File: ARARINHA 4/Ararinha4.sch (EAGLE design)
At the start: 105 parts, among them IC1 4053N, Q1 BC548, Q2 BC548, Q3 BC548, Q4 BC548, Q5 BC548, Q6 BC548, T1 TOROID-T37-4PIN, T2 TOROID-T37-4PIN, U1 LM386

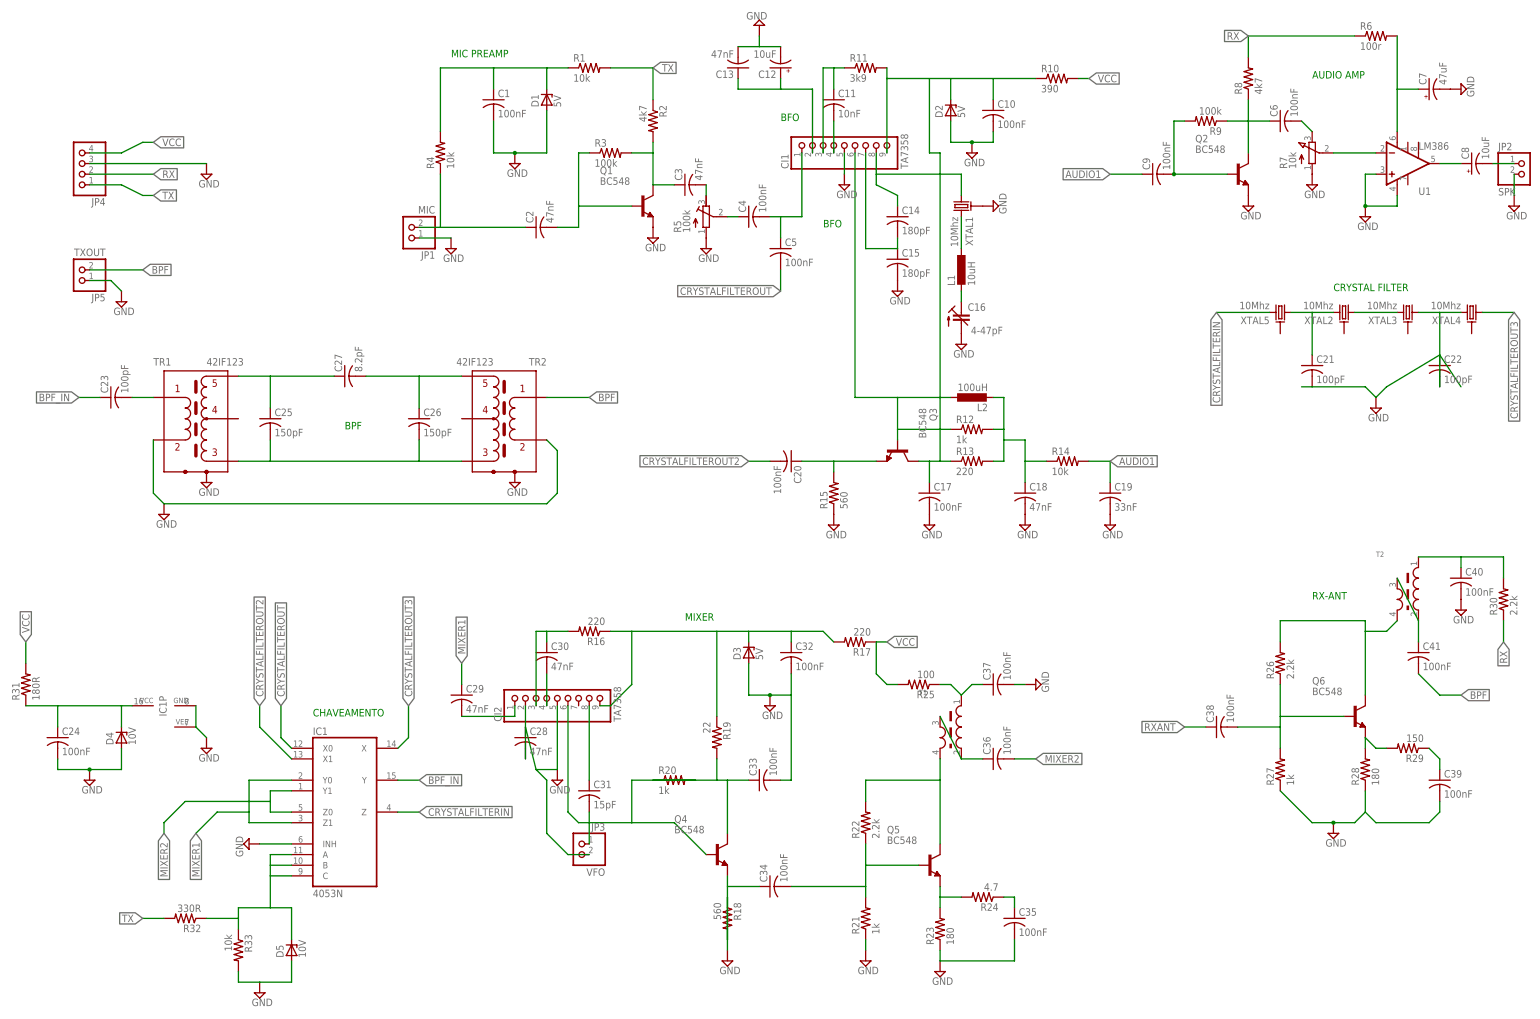
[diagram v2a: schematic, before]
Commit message: 
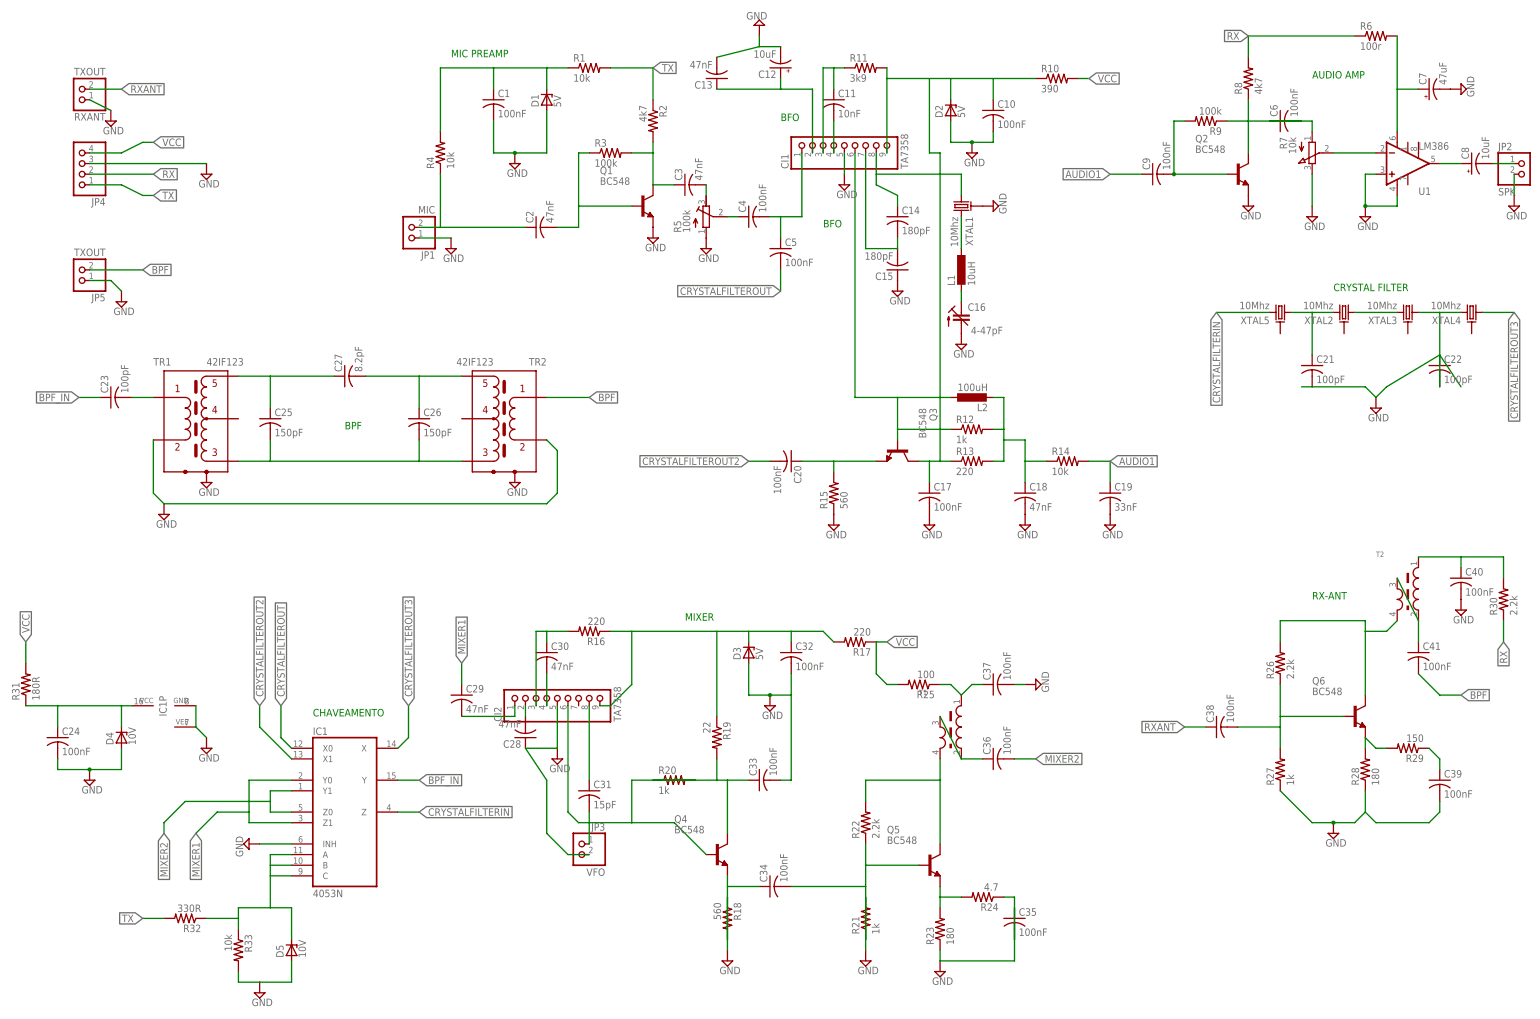
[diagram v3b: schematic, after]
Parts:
- added RXANT: TXOUT, pinhead:PINHD-1X2
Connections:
- removed net N$13 (its old number): C6.2, R7.E
- new net N$10: C6.1, R7.A
- net GND: now also C15.1, C35.1, R21.2, R7.E, RXANT.1; no longer C15.2, C35.2, R21.1, R7.A
- net N$14: now also C6.2; no longer C6.1
- net N$21: now also C15.2; no longer C15.1
- net N$43: now also C35.2; no longer C35.1
- net N$46: now also R21.1; no longer R21.2
- net RXANT: now also RXANT.2
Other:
- moved on the sheet: C13, C15, C28, R7
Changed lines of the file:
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@@
 <part name="SUPPLY36" library="supply2" deviceset="GND" device=""/>
 <part name="SUPPLY37" library="supply2" deviceset="GND" device=""/>
+<part name="RXANT" library="pinhead" deviceset="PINHD-1X2" device="" value="TXOUT"/>
+<part name="SUPPLY38" library="supply2" deviceset="GND" device=""/>
 </parts>
 <sheets>
@@
 <instance part="R6" gate="G$1" x="162.56" y="99.06"/>
 <instance part="C6" gate="G$1" x="139.7" y="78.74" rot="R90"/>
-<instance part="R7" gate="G$1" x="147.32" y="71.12"/>
+<instance part="R7" gate="G$1" x="147.32" y="71.12" rot="MR180"/>
 <instance part="C7" gate="G$1" x="175.26" y="86.36" rot="R90"/>
 <instance part="SUPPLY6" gate="GND" x="182.88" y="86.36" rot="R90"/>
@@
 <instance part="R9" gate="G$1" x="121.92" y="78.74" rot="R180"/>
 <instance part="SUPPLY8" gate="GND" x="132.08" y="58.42"/>
-<instance part="SUPPLY9" gate="GND" x="147.32" y="63.5"/>
+<instance part="SUPPLY9" gate="GND" x="147.32" y="55.88"/>
 <instance part="C9" gate="G$1" x="109.22" y="66.04" rot="R90"/>
 <instance part="D2" gate="G$1" x="60.96" y="81.28" rot="R90"/>
@@
 <instance part="C11" gate="G$1" x="33.02" y="83.82"/>
 <instance part="C12" gate="G$1" x="20.32" y="91.44" rot="R180"/>
-<instance part="C13" gate="G$1" x="10.16" y="91.44" rot="R180"/>
+<instance part="C13" gate="G$1" x="5.08" y="88.9" rot="R180"/>
 <instance part="SUPPLY11" gate="GND" x="35.56" y="63.5"/>
 <instance part="SUPPLY12" gate="GND" x="15.24" y="101.6" rot="R180"/>
 <instance part="C14" gate="G$1" x="48.26" y="55.88"/>
-<instance part="C15" gate="G$1" x="48.26" y="45.72"/>
+<instance part="C15" gate="G$1" x="48.26" y="43.18" rot="R180"/>
 <instance part="SUPPLY13" gate="GND" x="48.26" y="38.1"/>
 <instance part="L1" gate="G$1" x="63.5" y="43.18"/>
@@
 <instance part="C27" gate="G$1" x="-83.82" y="17.78" rot="R90"/>
 <instance part="CI2" gate="A" x="-33.02" y="-58.42" rot="R90"/>
-<instance part="SUPPLY22" gate="GND" x="-33.02" y="-78.74"/>
-<instance part="C28" gate="G$1" x="-40.64" y="-68.58"/>
+<instance part="SUPPLY22" gate="GND" x="-33.02" y="-73.66"/>
+<instance part="C28" gate="G$1" x="-40.64" y="-68.58" rot="R180"/>
 <instance part="C29" gate="G$1" x="-55.88" y="-58.42"/>
 <instance part="C30" gate="G$1" x="-35.56" y="-48.26"/>
@@
 <instance part="SUPPLY36" gate="GND" x="-116.84" y="-7.62"/>
 <instance part="SUPPLY37" gate="GND" x="-43.18" y="-7.62"/>
+<instance part="RXANT" gate="G$1" x="-147.32" y="86.36" rot="R180"/>
+<instance part="SUPPLY38" gate="GND" x="-139.7" y="78.74"/>
 </instances>
 <busses>
@@
 </segment>
 <segment>
-<pinref part="R7" gate="G$1" pin="A"/>
-<pinref part="SUPPLY9" gate="GND" pin="GND"/>
-</segment>
-<segment>
 <pinref part="D2" gate="G$1" pin="A"/>
 <wire x1="60.96" y1="78.74" x2="60.96" y2="73.66" width="0.1524" layer="91"/>
@@
 <pinref part="C13" gate="G$1" pin="2"/>
 <pinref part="SUPPLY12" gate="GND" pin="GND"/>
-<wire x1="10.16" y1="96.52" x2="15.24" y2="96.52" width="0.1524" layer="91"/>
+<wire x1="5.08" y1="93.98" x2="15.24" y2="96.52" width="0.1524" layer="91"/>
 <wire x1="15.24" y1="96.52" x2="15.24" y2="99.06" width="0.1524" layer="91"/>
 <pinref part="C12" gate="G$1" pin="-"/>
@@
 </segment>
 <segment>
-<pinref part="C15" gate="G$1" pin="2"/>
+<pinref part="C15" gate="G$1" pin="1"/>
 <pinref part="SUPPLY13" gate="GND" pin="GND"/>
 </segment>
@@
 <pinref part="CI2" gate="A" pin="5"/>
 <pinref part="SUPPLY22" gate="GND" pin="GND"/>
-<wire x1="-33.02" y1="-76.2" x2="-33.02" y2="-60.96" width="0.1524" layer="91"/>
+<wire x1="-33.02" y1="-71.12" x2="-33.02" y2="-60.96" width="0.1524" layer="91"/>
 <pinref part="C28" gate="G$1" pin="1"/>
-<wire x1="-40.64" y1="-66.04" x2="-38.1" y2="-76.2" width="0.1524" layer="91"/>
-<wire x1="-38.1" y1="-76.2" x2="-33.02" y2="-76.2" width="0.1524" layer="91"/>
+<wire x1="-40.64" y1="-71.12" x2="-33.02" y2="-71.12" width="0.1524" layer="91"/>
 <pinref part="JP3" gate="G$1" pin="2"/>
 <wire x1="-25.4" y1="-96.52" x2="-30.48" y2="-96.52" width="0.1524" layer="91"/>
 <wire x1="-30.48" y1="-96.52" x2="-35.56" y2="-91.44" width="0.1524" layer="91"/>
 <wire x1="-35.56" y1="-91.44" x2="-35.56" y2="-78.74" width="0.1524" layer="91"/>
-<wire x1="-35.56" y1="-78.74" x2="-38.1" y2="-76.2" width="0.1524" layer="91"/>
+<wire x1="-35.56" y1="-78.74" x2="-40.64" y2="-71.12" width="0.1524" layer="91"/>
 </segment>
 <segment>
@@
 </segment>
 <segment>
-<pinref part="R21" gate="G$1" pin="1"/>
+<pinref part="R21" gate="G$1" pin="2"/>
 <pinref part="SUPPLY25" gate="GND" pin="GND"/>
-<wire x1="40.64" y1="-119.38" x2="40.64" y2="-116.84" width="0.1524" layer="91"/>
+<wire x1="40.64" y1="-119.38" x2="40.64" y2="-106.68" width="0.1524" layer="91"/>
 </segment>
 <segment>
@@
 <pinref part="SUPPLY26" gate="GND" pin="GND"/>
 <wire x1="58.42" y1="-121.92" x2="58.42" y2="-119.38" width="0.1524" layer="91"/>
-<pinref part="C35" gate="G$1" pin="2"/>
-<wire x1="76.2" y1="-116.84" x2="76.2" y2="-121.92" width="0.1524" layer="91"/>
+<pinref part="C35" gate="G$1" pin="1"/>
+<wire x1="76.2" y1="-109.22" x2="76.2" y2="-121.92" width="0.1524" layer="91"/>
 <wire x1="76.2" y1="-121.92" x2="58.42" y2="-121.92" width="0.1524" layer="91"/>
 </segment>
@@
 <pinref part="SUPPLY37" gate="GND" pin="GND"/>
 </segment>
+<segment>
+<pinref part="R7" gate="G$1" pin="E"/>
+<pinref part="SUPPLY9" gate="GND" pin="GND"/>
+<wire x1="147.32" y1="66.04" x2="147.32" y2="58.42" width="0.1524" layer="91"/>
+</segment>
+<segment>
+<pinref part="RXANT" gate="G$1" pin="1"/>
+<pinref part="SUPPLY38" gate="GND" pin="GND"/>
+<wire x1="-139.7" y1="81.28" x2="-144.78" y2="83.82" width="0.1524" layer="91"/>
+</segment>
 </net>
 <net name="TX" class="0">
@@
 </segment>
 </net>
-<net name="N$10" class="0">
-<segment>
-<pinref part="R7" gate="G$1" pin="S"/>
-<pinref part="U1" gate="G$1" pin="-IN"/>
-<wire x1="152.4" y1="71.12" x2="162.56" y2="71.12" width="0.1524" layer="91"/>
-</segment>
-</net>
 <net name="N$11" class="0">
 <segment>
@@
 </segment>
 </net>
-<net name="N$13" class="0">
-<segment>
-<pinref part="R7" gate="G$1" pin="E"/>
-<pinref part="C6" gate="G$1" pin="2"/>
-<wire x1="144.78" y1="78.74" x2="147.32" y2="76.2" width="0.1524" layer="91"/>
-</segment>
-</net>
 <net name="N$14" class="0">
 <segment>
 <pinref part="Q2" gate="G$1" pin="C"/>
 <wire x1="132.08" y1="71.12" x2="132.08" y2="78.74" width="0.1524" layer="91"/>
-<pinref part="C6" gate="G$1" pin="1"/>
-<wire x1="132.08" y1="78.74" x2="137.16" y2="78.74" width="0.1524" layer="91"/>
 <pinref part="R8" gate="G$1" pin="1"/>
 <wire x1="132.08" y1="83.82" x2="132.08" y2="78.74" width="0.1524" layer="91"/>
 <pinref part="R9" gate="G$1" pin="1"/>
 <wire x1="127" y1="78.74" x2="132.08" y2="78.74" width="0.1524" layer="91"/>
+<pinref part="C6" gate="G$1" pin="2"/>
+<wire x1="144.78" y1="78.74" x2="132.08" y2="78.74" width="0.1524" layer="91"/>
 </segment>
 </net>
@@
 <segment>
 <pinref part="C13" gate="G$1" pin="1"/>
-<wire x1="10.16" y1="88.9" x2="10.16" y2="86.36" width="0.1524" layer="91"/>
 <pinref part="C12" gate="G$1" pin="+"/>
-<wire x1="10.16" y1="86.36" x2="20.32" y2="86.36" width="0.1524" layer="91"/>
+<wire x1="5.08" y1="86.36" x2="20.32" y2="86.36" width="0.1524" layer="91"/>
 <wire x1="20.32" y1="86.36" x2="20.32" y2="88.9" width="0.1524" layer="91"/>
 <pinref part="CI1" gate="A" pin="2"/>
@@
 <segment>
 <pinref part="C14" gate="G$1" pin="2"/>
-<pinref part="C15" gate="G$1" pin="1"/>
+<pinref part="C15" gate="G$1" pin="2"/>
 <wire x1="48.26" y1="50.8" x2="48.26" y2="48.26" width="0.1524" layer="91"/>
 <pinref part="CI1" gate="A" pin="7"/>
@@
 <pinref part="CI2" gate="A" pin="2"/>
 <pinref part="C28" gate="G$1" pin="2"/>
-<wire x1="-40.64" y1="-73.66" x2="-40.64" y2="-60.96" width="0.1524" layer="91"/>
+<wire x1="-40.64" y1="-63.5" x2="-40.64" y2="-60.96" width="0.1524" layer="91"/>
 </segment>
 </net>
@@
 <net name="N$46" class="0">
 <segment>
-<pinref part="R21" gate="G$1" pin="2"/>
+<pinref part="R21" gate="G$1" pin="1"/>
 <pinref part="R22" gate="G$1" pin="1"/>
-<wire x1="40.64" y1="-106.68" x2="40.64" y2="-104.14" width="0.1524" layer="91"/>
+<wire x1="40.64" y1="-116.84" x2="40.64" y2="-104.14" width="0.1524" layer="91"/>
 <pinref part="C34" gate="G$1" pin="2"/>
 <wire x1="40.64" y1="-99.06" x2="40.64" y2="-93.98" width="0.1524" layer="91"/>
@@
 <segment>
 <pinref part="R24" gate="G$1" pin="1"/>
-<pinref part="C35" gate="G$1" pin="1"/>
+<pinref part="C35" gate="G$1" pin="2"/>
 <wire x1="73.66" y1="-106.68" x2="76.2" y2="-106.68" width="0.1524" layer="91"/>
-<wire x1="76.2" y1="-106.68" x2="76.2" y2="-109.22" width="0.1524" layer="91"/>
+<wire x1="76.2" y1="-106.68" x2="76.2" y2="-116.84" width="0.1524" layer="91"/>
 </segment>
 </net>
@@
 <wire x1="121.92" y1="-66.04" x2="116.84" y2="-66.04" width="0.1524" layer="91"/>
 <label x="116.84" y="-66.04" size="1.778" layer="95" rot="R180" xref="yes"/>
+</segment>
+<segment>
+<pinref part="RXANT" gate="G$1" pin="2"/>
+<wire x1="-144.78" y1="86.36" x2="-137.16" y2="86.36" width="0.1524" layer="91"/>
+<label x="-137.16" y="86.36" size="1.778" layer="95" xref="yes"/>
 </segment>
 </net>
@@
 </segment>
 </net>
+<net name="N$10" class="0">
+<segment>
+<pinref part="C6" gate="G$1" pin="1"/>
+<pinref part="R7" gate="G$1" pin="A"/>
+<wire x1="137.16" y1="78.74" x2="147.32" y2="78.74" width="0.1524" layer="91"/>
+<wire x1="147.32" y1="78.74" x2="147.32" y2="76.2" width="0.1524" layer="91"/>
+</segment>
+</net>
+<net name="N$13" class="0">
+<segment>
+<pinref part="R7" gate="G$1" pin="S"/>
+<pinref part="U1" gate="G$1" pin="-IN"/>
+<wire x1="152.4" y1="71.12" x2="162.56" y2="71.12" width="0.1524" layer="91"/>
+</segment>
+</net>
